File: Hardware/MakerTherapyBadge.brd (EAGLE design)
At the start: 63.5 x 85.7 mm, 69 parts, among them J1 AVR_SPI_PROG_3X2NS, U1 ATMEGA328P_TQFP, U3 MCP73831.SOT23-5

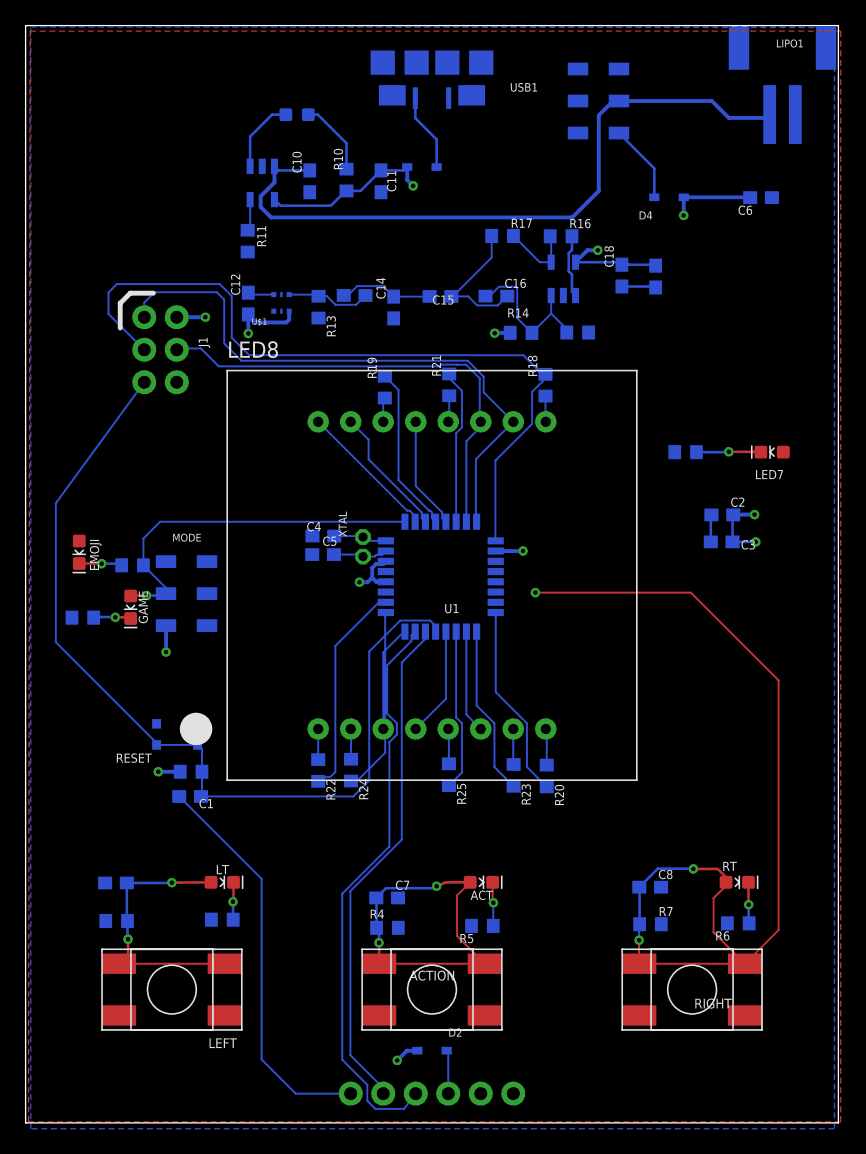
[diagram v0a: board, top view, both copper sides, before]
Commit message: connected buttons
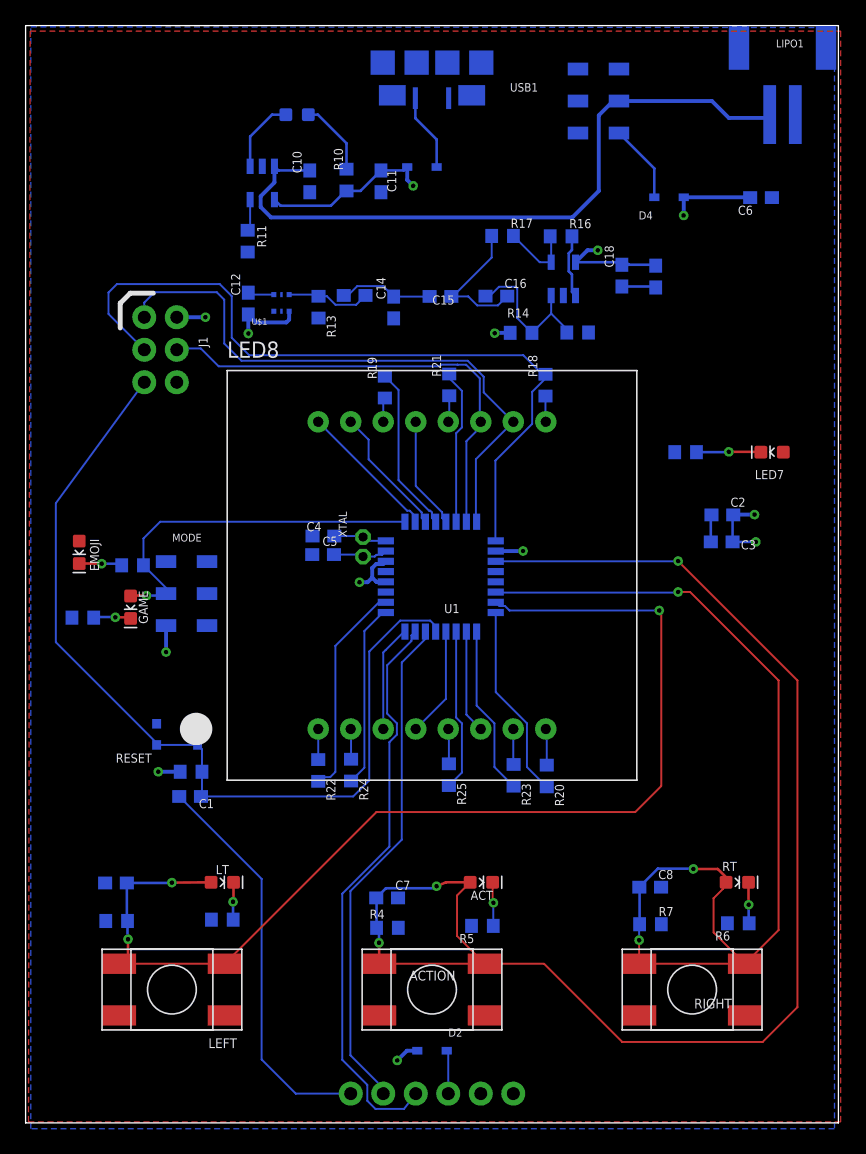
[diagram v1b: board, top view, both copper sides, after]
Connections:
- removed net N$15: C9.1, LEFT.3, LEFT.4, LT.A, R8.2
- removed net N$16: ACT.A, ACTION.3, ACTION.4, C7.2, R4.2
- removed net N$19: C8.2, R7.2, RIGHT.3, RIGHT.4, RT.A
- net ACTION: now also ACT.A, ACTION.3, ACTION.4, C7.2, R4.2
- net LEFT: now also C9.1, LEFT.3, LEFT.4, LT.A, R8.2
- net RIGHT: now also C8.2, R7.2, RIGHT.3, RIGHT.4, RT.A
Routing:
- net ACTION: track 0.00 -> 110.0 mm, vias 0 -> 3
- net LEFT: track 0.00 -> 88.0 mm, vias 0 -> 3
- net RIGHT: track 0.00 -> 78.3 mm, vias 0 -> 3
- net N$19: track 75.1 -> 0.00 mm, vias 3 -> 0
- net N$16: track 29.0 -> 0.00 mm, vias 2 -> 0
- net N$15: track 21.2 -> 0.00 mm, vias 2 -> 0
